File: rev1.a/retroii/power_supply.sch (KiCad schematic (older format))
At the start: 40 parts, among them J10 BARREL_JACK, J11 Conn_02x10_Counter_Clockwise, SW2 SPST2, U11 LM2576-12, U12 LM2576-5, U13 LM2576-12, U14 LM2576-3.3, U15 LM2576-5

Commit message: added vga dsub-15 footprint and 3d model
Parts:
- SW2: footprint 6502Library:SW_Micro_Right_Angle_SPST -> retroii_footprints:SW_Micro_Right_Angle_SPST
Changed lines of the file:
@@
 F 0 "SW2" H 2215 1280 50  0000 C CNN
 F 1 "SPST2" H 2215 1080 50  0000 C CNN
-F 2 "6502Library:SW_Micro_Right_Angle_SPST" H 2215 1180 50  0001 C CNN
+F 2 "retroii_footprints:SW_Micro_Right_Angle_SPST" H 2215 1180 50  0001 C CNN
 F 3 "" H 2215 1180 50  0000 C CNN
 	1    2215 1180

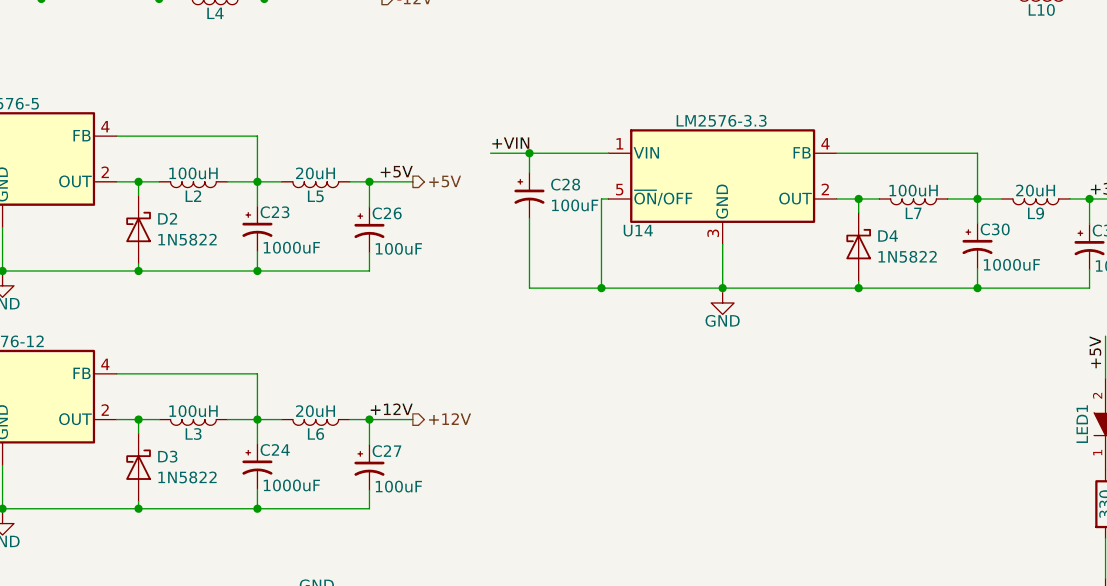
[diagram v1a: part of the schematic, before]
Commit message: added 3d model/footprints for 100uH and 20uH inductors.
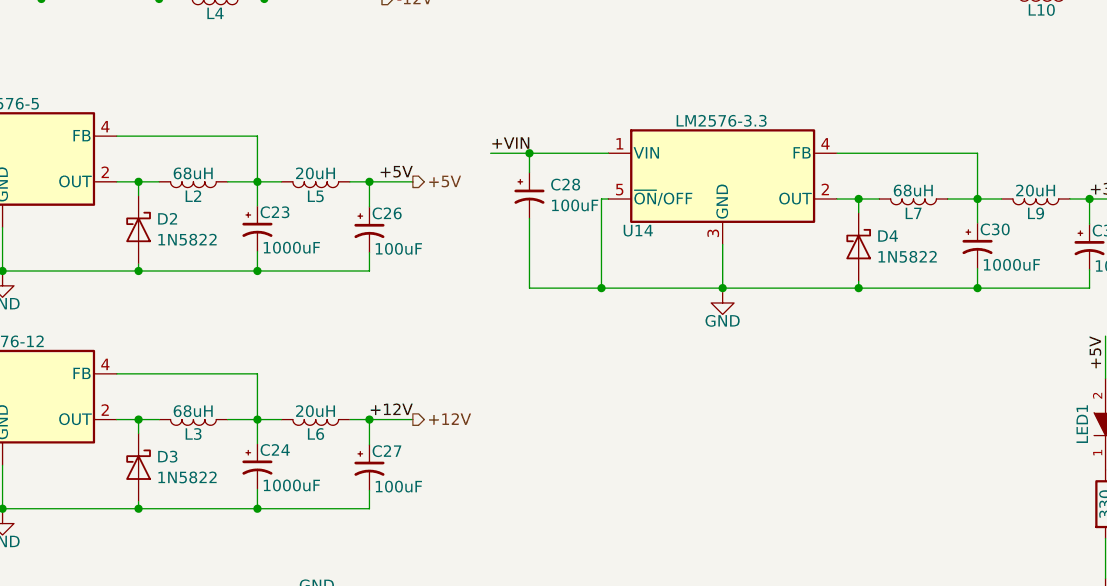
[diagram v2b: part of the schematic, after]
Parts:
- L1, L8: footprint (none) -> retroii_footprints:Bourns_SRP1770TA-101M
- L10, L4, L5, L6, L9: footprint (none) -> retroii_footprints:Pulse_PF0382.223NLT
- L2, L3, L7: value 100uH -> 68uH; footprint (none) -> retroii_footprints:Bourns_SRP1770TA-101M
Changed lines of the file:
@@
 F 0 "L1" V 3835 2315 50  0000 C CNN
 F 1 "68uH" V 3735 2315 50  0000 C CNN
-F 2 "" H 3770 2315 50  0001 C CNN
+F 2 "retroii_footprints:Bourns_SRP1770TA-101M" H 3770 2315 50  0001 C CNN
 F 3 "~" H 3770 2315 50  0001 C CNN
 	1    3770 2315
@@
 P 4170 3805
 F 0 "L2" V 4235 3805 50  0000 C CNN
-F 1 "100uH" V 4135 3805 50  0000 C CNN
-F 2 "" H 4170 3805 50  0001 C CNN
+F 1 "68uH" V 4135 3805 50  0000 C CNN
+F 2 "retroii_footprints:Bourns_SRP1770TA-101M" H 4170 3805 50  0001 C CNN
 F 3 "~" H 4170 3805 50  0001 C CNN
 	1    4170 3805
@@
 F 0 "L5" V 4770 3805 50  0000 C CNN
 F 1 "20uH" V 4670 3805 50  0000 C CNN
-F 2 "" H 4705 3805 50  0001 C CNN
+F 2 "retroii_footprints:Pulse_PF0382.223NLT" H 4705 3805 50  0001 C CNN
 F 3 "~" H 4705 3805 50  0001 C CNN
 	1    4705 3805
@@
 P 4170 4845
 F 0 "L3" V 4235 4845 50  0000 C CNN
-F 1 "100uH" V 4135 4845 50  0000 C CNN
-F 2 "" H 4170 4845 50  0001 C CNN
+F 1 "68uH" V 4135 4845 50  0000 C CNN
+F 2 "retroii_footprints:Bourns_SRP1770TA-101M" H 4170 4845 50  0001 C CNN
 F 3 "~" H 4170 4845 50  0001 C CNN
 	1    4170 4845
@@
 F 0 "L6" V 4770 4845 50  0000 C CNN
 F 1 "20uH" V 4670 4845 50  0000 C CNN
-F 2 "" H 4705 4845 50  0001 C CNN
+F 2 "retroii_footprints:Pulse_PF0382.223NLT" H 4705 4845 50  0001 C CNN
 F 3 "~" H 4705 4845 50  0001 C CNN
 	1    4705 4845
@@
 F 0 "L8" V 7450 2300 50  0000 C CNN
 F 1 "68uH" V 7350 2300 50  0000 C CNN
-F 2 "" H 7385 2300 50  0001 C CNN
+F 2 "retroii_footprints:Bourns_SRP1770TA-101M" H 7385 2300 50  0001 C CNN
 F 3 "~" H 7385 2300 50  0001 C CNN
 	1    7385 2300
@@
 P 7320 3880
 F 0 "L7" V 7385 3880 50  0000 C CNN
-F 1 "100uH" V 7285 3880 50  0000 C CNN
-F 2 "" H 7320 3880 50  0001 C CNN
+F 1 "68uH" V 7285 3880 50  0000 C CNN
+F 2 "retroii_footprints:Bourns_SRP1770TA-101M" H 7320 3880 50  0001 C CNN
 F 3 "~" H 7320 3880 50  0001 C CNN
 	1    7320 3880
@@
 F 0 "L9" V 7920 3880 50  0000 C CNN
 F 1 "20uH" V 7820 3880 50  0000 C CNN
-F 2 "" H 7855 3880 50  0001 C CNN
+F 2 "retroii_footprints:Pulse_PF0382.223NLT" H 7855 3880 50  0001 C CNN
 F 3 "~" H 7855 3880 50  0001 C CNN
 	1    7855 3880
@@
 F 0 "L10" V 7945 2990 50  0000 C CNN
 F 1 "20uH" V 7775 2985 50  0000 C CNN
-F 2 "" H 7880 2990 50  0001 C CNN
+F 2 "retroii_footprints:Pulse_PF0382.223NLT" H 7880 2990 50  0001 C CNN
 F 3 "~" H 7880 2990 50  0001 C CNN
 	1    7880 2990
@@
 F 0 "L4" V 4330 3005 50  0000 C CNN
 F 1 "20uH" V 4160 3000 50  0000 C CNN
-F 2 "" H 4265 3005 50  0001 C CNN
+F 2 "retroii_footprints:Pulse_PF0382.223NLT" H 4265 3005 50  0001 C CNN
 F 3 "~" H 4265 3005 50  0001 C CNN
 	1    4265 3005

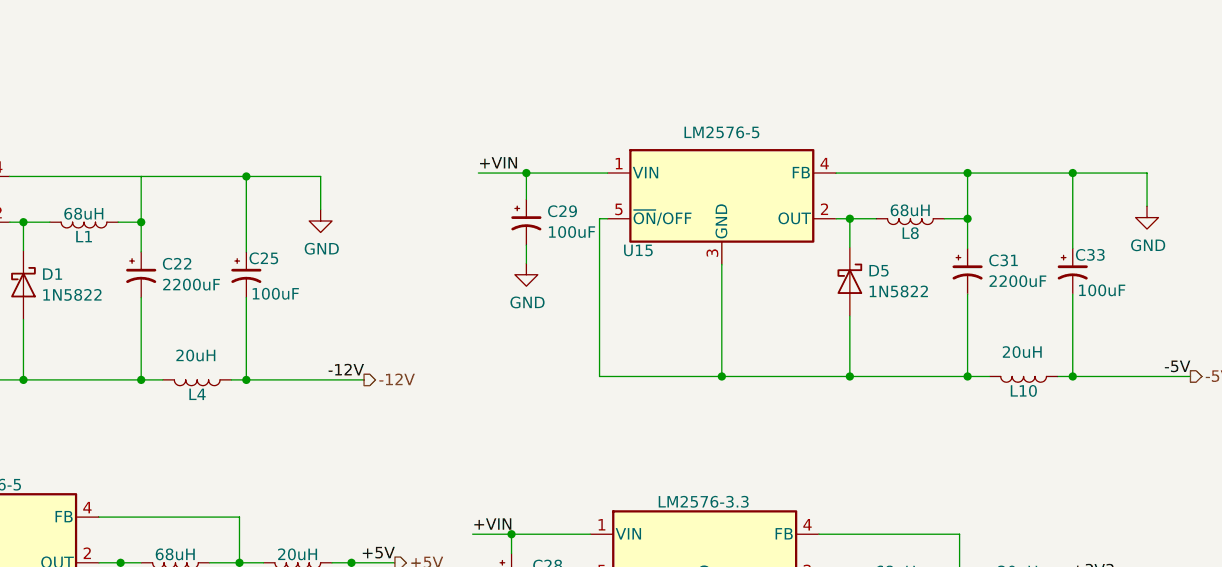
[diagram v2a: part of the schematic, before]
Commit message: finished footprints/models for power supply caps
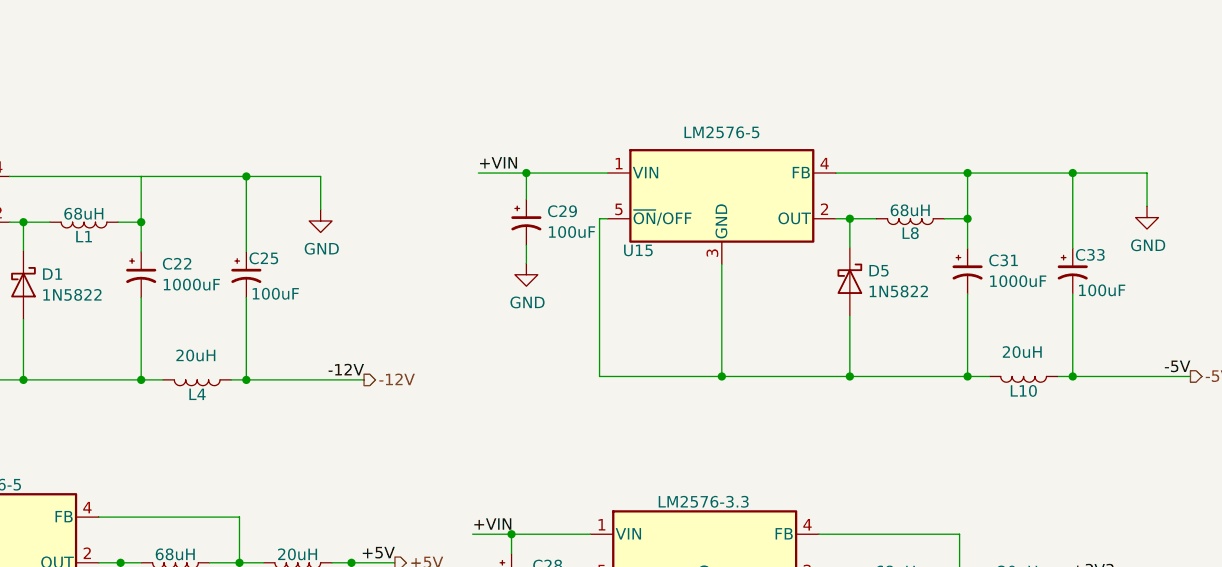
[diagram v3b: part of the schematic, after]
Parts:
- C19, C20, C21, C25, C26, C27, C28, C29, C32, C33: footprint (none) -> Capacitor_THT:CP_Radial_D8.0mm_P3.50mm
- C22, C31: value 2200uF -> 1000uF; footprint (none) -> Capacitor_THT:CP_Radial_D13.0mm_P5.00mm
- C23, C24, C30: footprint (none) -> Capacitor_THT:CP_Radial_D13.0mm_P5.00mm
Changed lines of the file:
@@
 P 4020 2545
 F 0 "C22" H 4111 2591 50  0000 L CNN
-F 1 "2200uF" H 4111 2500 50  0000 L CNN
-F 2 "" H 4058 2395 50  0001 C CNN
+F 1 "1000uF" H 4111 2500 50  0000 L CNN
+F 2 "Capacitor_THT:CP_Radial_D13.0mm_P5.00mm" H 4058 2395 50  0001 C CNN
 F 3 "~" H 4020 2545 50  0001 C CNN
 	1    4020 2545
@@
 F 0 "C19" H 2181 2376 50  0000 L CNN
 F 1 "100uF" H 2181 2285 50  0000 L CNN
-F 2 "" H 2128 2180 50  0001 C CNN
+F 2 "Capacitor_THT:CP_Radial_D8.0mm_P3.50mm" H 2128 2180 50  0001 C CNN
 F 3 "~" H 2090 2330 50  0001 C CNN
 	1    2090 2330
@@
 F 0 "C23" H 4460 4080 50  0000 L CNN
 F 1 "1000uF" H 4470 3925 50  0000 L CNN
-F 2 "" H 4488 3860 50  0001 C CNN
+F 2 "Capacitor_THT:CP_Radial_D13.0mm_P5.00mm" H 4488 3860 50  0001 C CNN
 F 3 "~" H 4450 4010 50  0001 C CNN
 	1    4450 4010
@@
 F 0 "C20" H 2581 3836 50  0000 L CNN
 F 1 "100uF" H 2581 3745 50  0000 L CNN
-F 2 "" H 2528 3640 50  0001 C CNN
+F 2 "Capacitor_THT:CP_Radial_D8.0mm_P3.50mm" H 2528 3640 50  0001 C CNN
 F 3 "~" H 2490 3790 50  0001 C CNN
 	1    2490 3790
@@
 F 0 "C26" H 4950 4085 50  0000 L CNN
 F 1 "100uF" H 4960 3930 50  0000 L CNN
-F 2 "" H 4978 3865 50  0001 C CNN
+F 2 "Capacitor_THT:CP_Radial_D8.0mm_P3.50mm" H 4978 3865 50  0001 C CNN
 F 3 "~" H 4940 4015 50  0001 C CNN
 	1    4940 4015
@@
 F 0 "C24" H 4460 5120 50  0000 L CNN
 F 1 "1000uF" H 4470 4965 50  0000 L CNN
-F 2 "" H 4488 4900 50  0001 C CNN
+F 2 "Capacitor_THT:CP_Radial_D13.0mm_P5.00mm" H 4488 4900 50  0001 C CNN
 F 3 "~" H 4450 5050 50  0001 C CNN
 	1    4450 5050
@@
 F 0 "C21" H 2581 4876 50  0000 L CNN
 F 1 "100uF" H 2581 4785 50  0000 L CNN
-F 2 "" H 2528 4680 50  0001 C CNN
+F 2 "Capacitor_THT:CP_Radial_D8.0mm_P3.50mm" H 2528 4680 50  0001 C CNN
 F 3 "~" H 2490 4830 50  0001 C CNN
 	1    2490 4830
@@
 F 0 "C27" H 4950 5125 50  0000 L CNN
 F 1 "100uF" H 4960 4970 50  0000 L CNN
-F 2 "" H 4978 4905 50  0001 C CNN
+F 2 "Capacitor_THT:CP_Radial_D8.0mm_P3.50mm" H 4978 4905 50  0001 C CNN
 F 3 "~" H 4940 5055 50  0001 C CNN
 	1    4940 5055
@@
 P 7635 2530
 F 0 "C31" H 7726 2576 50  0000 L CNN
-F 1 "2200uF" H 7726 2485 50  0000 L CNN
-F 2 "" H 7673 2380 50  0001 C CNN
+F 1 "1000uF" H 7726 2485 50  0000 L CNN
+F 2 "Capacitor_THT:CP_Radial_D13.0mm_P5.00mm" H 7673 2380 50  0001 C CNN
 F 3 "~" H 7635 2530 50  0001 C CNN
 	1    7635 2530
@@
 F 0 "C29" H 5796 2361 50  0000 L CNN
 F 1 "100uF" H 5796 2270 50  0000 L CNN
-F 2 "" H 5743 2165 50  0001 C CNN
+F 2 "Capacitor_THT:CP_Radial_D8.0mm_P3.50mm" H 5743 2165 50  0001 C CNN
 F 3 "~" H 5705 2315 50  0001 C CNN
 	1    5705 2315
@@
 F 0 "C30" H 7610 4155 50  0000 L CNN
 F 1 "1000uF" H 7620 4000 50  0000 L CNN
-F 2 "" H 7638 3935 50  0001 C CNN
+F 2 "Capacitor_THT:CP_Radial_D13.0mm_P5.00mm" H 7638 3935 50  0001 C CNN
 F 3 "~" H 7600 4085 50  0001 C CNN
 	1    7600 4085
@@
 F 0 "C28" H 5731 3911 50  0000 L CNN
 F 1 "100uF" H 5731 3820 50  0000 L CNN
-F 2 "" H 5678 3715 50  0001 C CNN
+F 2 "Capacitor_THT:CP_Radial_D8.0mm_P3.50mm" H 5678 3715 50  0001 C CNN
 F 3 "~" H 5640 3865 50  0001 C CNN
 	1    5640 3865
@@
 F 0 "C32" H 8100 4160 50  0000 L CNN
 F 1 "100uF" H 8110 4005 50  0000 L CNN
-F 2 "" H 8128 3940 50  0001 C CNN
+F 2 "Capacitor_THT:CP_Radial_D8.0mm_P3.50mm" H 8128 3940 50  0001 C CNN
 F 3 "~" H 8090 4090 50  0001 C CNN
 	1    8090 4090
@@
 F 0 "C33" H 8105 2600 50  0000 L CNN
 F 1 "100uF" H 8115 2445 50  0000 L CNN
-F 2 "" H 8133 2380 50  0001 C CNN
+F 2 "Capacitor_THT:CP_Radial_D8.0mm_P3.50mm" H 8133 2380 50  0001 C CNN
 F 3 "~" H 8095 2530 50  0001 C CNN
 	1    8095 2530
@@
 F 0 "C25" H 4490 2615 50  0000 L CNN
 F 1 "100uF" H 4500 2460 50  0000 L CNN
-F 2 "" H 4518 2395 50  0001 C CNN
+F 2 "Capacitor_THT:CP_Radial_D8.0mm_P3.50mm" H 4518 2395 50  0001 C CNN
 F 3 "~" H 4480 2545 50  0001 C CNN
 	1    4480 2545

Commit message: footprint finalizations.
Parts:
- J11: value Conn_02x10_Counter_Clockwise -> Conn_02x10; symbol Connector_Generic:Conn_02x10_Counter_Clockwise -> Connector_Generic:Conn_02x10_Odd_Even
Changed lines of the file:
@@
 Connection ~ 7600 4270
 $Comp
-L Connector_Generic:Conn_02x10_Counter_Clockwise J11
+L Connector_Generic:Conn_02x10_Odd_Even J11
 U 1 1 5CAAD78B
 P 4765 6180
 F 0 "J11" V 4769 6660 50  0000 L CNN
-F 1 "Conn_02x10_Counter_Clockwise" V 4860 6660 50  0000 L CNN
+F 1 "Conn_02x10" V 4860 6660 50  0000 L CNN
 F 2 "Connector_PinSocket_2.54mm:PinSocket_2x10_P2.54mm_Vertical" H 4765 6180 50  0001 C CNN
 F 3 "~" H 4765 6180 50  0001 C CNN

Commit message: replaced 558 quad timer with 2 556 dual timers.
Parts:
- U11, U15: footprint Package_TO_SOT_THT:TO-220-5_Vertical -> retroii_footprints:TO-220-5_Horizontal_TabDown
- U12, U13, U14: footprint Package_TO_SOT_SMD:TO-263-5_TabPin3 -> retroii_footprints:TO-220-5_Horizontal_TabDown
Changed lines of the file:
@@
 F 0 "U11" H 2580 1975 50  0000 C CNN
 F 1 "LM2576-12" H 2945 2491 50  0000 C CNN
-F 2 "Package_TO_SOT_THT:TO-220-5_Vertical" H 2945 1965 50  0001 L CIN
+F 2 "retroii_footprints:TO-220-5_Horizontal_TabDown" H 2945 1965 50  0001 L CIN
 F 3 "http://ww1.microchip.com/downloads/en/DeviceDoc/lm2575.pdf" H 2945 2215 50  0001 C CNN
 	1    2945 2215
@@
 F 0 "U12" H 2965 3465 50  0000 C CNN
 F 1 "LM2576-5" H 3330 3945 50  0000 C CNN
-F 2 "Package_TO_SOT_SMD:TO-263-5_TabPin3" H 3335 3455 50  0001 L CIN
+F 2 "retroii_footprints:TO-220-5_Horizontal_TabDown" H 3335 3455 50  0001 L CIN
 F 3 "http://www.ti.com/lit/ds/symlink/lm2576.pdf" H 3335 3705 50  0001 C CNN
 	1    3335 3705
@@
 F 0 "U13" H 2965 4505 50  0000 C CNN
 F 1 "LM2576-12" H 3330 4985 50  0000 C CNN
-F 2 "Package_TO_SOT_SMD:TO-263-5_TabPin3" H 3335 4495 50  0001 L CIN
+F 2 "retroii_footprints:TO-220-5_Horizontal_TabDown" H 3335 4495 50  0001 L CIN
 F 3 "http://www.ti.com/lit/ds/symlink/lm2576.pdf" H 3335 4745 50  0001 C CNN
 	1    3335 4745
@@
 F 0 "U15" H 6195 1960 50  0000 C CNN
 F 1 "LM2576-5" H 6560 2476 50  0000 C CNN
-F 2 "Package_TO_SOT_THT:TO-220-5_Vertical" H 6560 1950 50  0001 L CIN
+F 2 "retroii_footprints:TO-220-5_Horizontal_TabDown" H 6560 1950 50  0001 L CIN
 F 3 "http://ww1.microchip.com/downloads/en/DeviceDoc/lm2575.pdf" H 6560 2200 50  0001 C CNN
 	1    6560 2200
@@
 F 0 "U14" H 6115 3540 50  0000 C CNN
 F 1 "LM2576-3.3" H 6480 4020 50  0000 C CNN
-F 2 "Package_TO_SOT_SMD:TO-263-5_TabPin3" H 6485 3530 50  0001 L CIN
+F 2 "retroii_footprints:TO-220-5_Horizontal_TabDown" H 6485 3530 50  0001 L CIN
 F 3 "http://www.ti.com/lit/ds/symlink/lm2576.pdf" H 6485 3780 50  0001 C CNN
 	1    6485 3780
